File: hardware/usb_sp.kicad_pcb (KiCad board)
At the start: 4 copper layers, 38.1 x 59.7 mm, 48 parts, among them U1 CH32V203C8U6, U10 SN74LVC1G32DBVR, U2 ZD24C02B-MAGMT, U3 32.768kHz, U4 KH-TYPE-C-16P, U5 SD101CWS, U6 CH572D, U7 HX_JN1_27-2X5P_ZZ_H4_9, U8 HX_JN1_27-2X5P_ZZ_H4_9, U9 SN74LVC1G32DBVR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

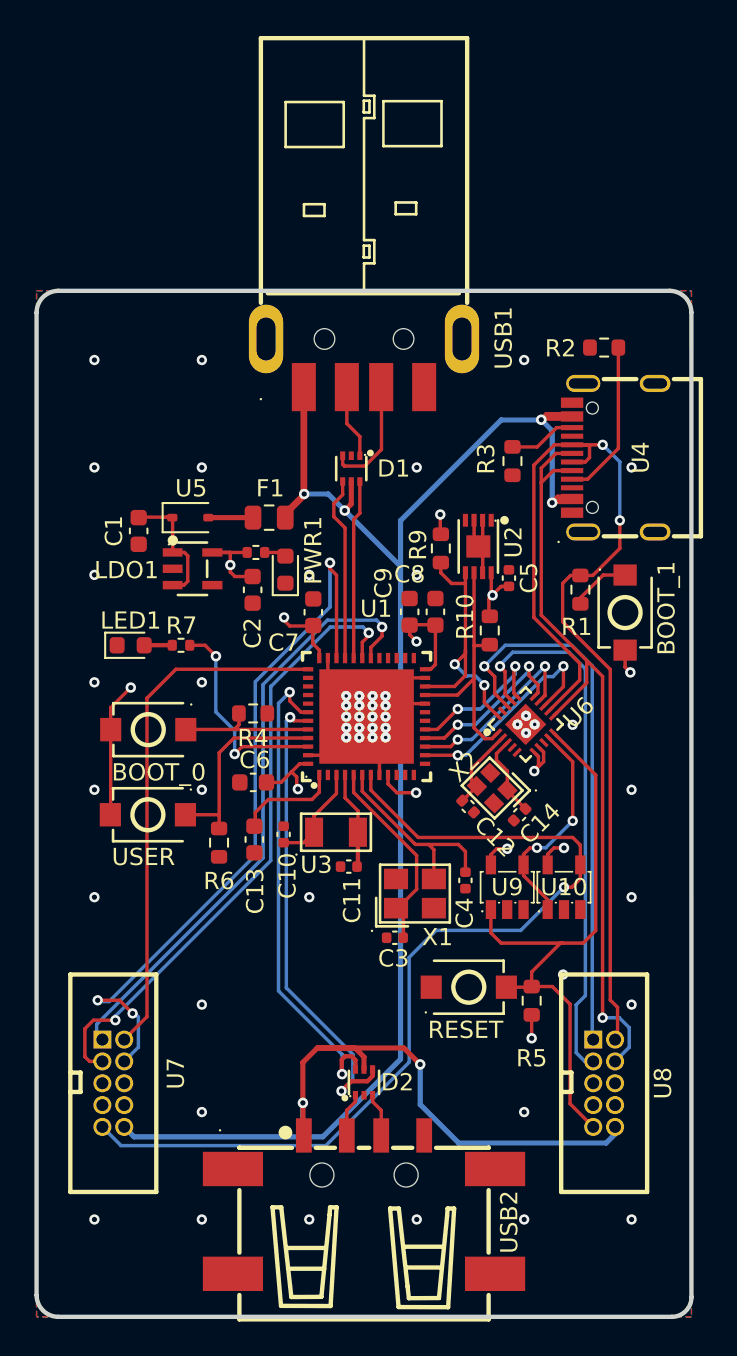
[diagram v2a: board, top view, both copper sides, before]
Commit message: style: improve trace paths
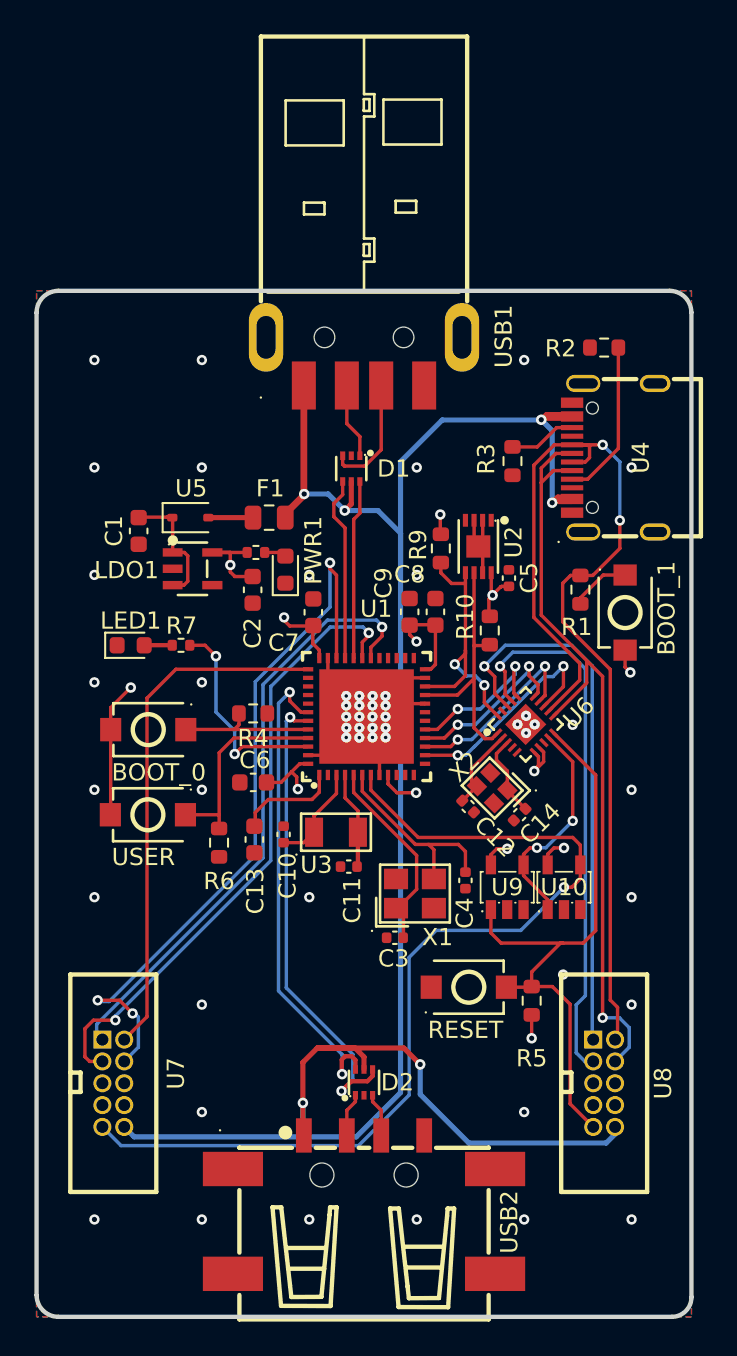
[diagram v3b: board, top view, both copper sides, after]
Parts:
- moved USB1 0.09 mm to (145.9, 70.9)
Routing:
- net VBUS: track 121.1 -> 125.6 mm
- net /CH32V203/RST_CH32: track 54.6 -> 55.7 mm
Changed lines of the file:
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@@
 	(footprint "usb_sp_fp:USB-A-SMD_917-181A102ES60200"
 		(layer "F.Cu")
-		(at 145.879523 70.956735 90)
+		(at 145.879523 70.863526 90)
 		(descr "USB-A-SMD_917-181A102ES60200 footprint")
 		(tags "USB-A-SMD_917-181A102ES60200 footprint C46394")
@@
 	)
 	(segment
-		(start 145.929523 76.950809)
-		(end 144.738727 76.950809)
-		(width 0.2)
-		(layer "F.Cu")
-		(net 40)
-	)
-	(segment
-		(start 146.895523 72.372735)
-		(end 146.895523 75.984809)
+		(start 146.879523 72.356735)
+		(end 146.879523 76.000809)
 		(width 0.2)
 		(layer "F.Cu")
@@
 	)
 	(segment
-		(start 146.900523 72.860335)
-		(end 146.879523 72.839335)
+		(start 144.638523 76.850605)
+		(end 144.638523 76.348745)
 		(width 0.2)
 		(layer "F.Cu")
@@
 	)
 	(segment
-		(start 146.879523 72.356735)
-		(end 146.895523 72.372735)
+		(start 146.879523 72.839335)
+		(end 146.879523 72.356735)
 		(width 0.2)
 		(layer "F.Cu")
@@
 	)
 	(segment
-		(start 146.879523 72.839335)
-		(end 146.879523 72.356735)
+		(start 144.738727 76.950809)
+		(end 144.638523 76.850605)
 		(width 0.2)
 		(layer "F.Cu")
@@
 	)
 	(segment
-		(start 144.638523 76.850605)
-		(end 144.638523 76.348745)
+		(start 146.900523 72.860335)
+		(end 146.879523 72.839335)
 		(width 0.2)
 		(layer "F.Cu")
@@
 	)
 	(segment
-		(start 144.738727 76.950809)
-		(end 144.638523 76.850605)
+		(start 146.879523 76.000809)
+		(end 145.929523 76.950809)
 		(width 0.2)
 		(layer "F.Cu")
@@
 	)
 	(segment
-		(start 146.895523 75.984809)
-		(end 145.929523 76.950809)
+		(start 145.929523 76.950809)
+		(end 144.738727 76.950809)
 		(width 0.2)
 		(layer "F.Cu")
@@
 	)
 	(segment
-		(start 144.879523 74.475809)
-		(end 144.879523 72.356735)
+		(start 145.638523 75.234809)
+		(end 144.879523 74.475809)
 		(width 0.2)
 		(layer "F.Cu")
@@
 	)
 	(segment
-		(start 145.638523 75.234809)
-		(end 144.879523 74.475809)
+		(start 144.879523 74.475809)
+		(end 144.879523 72.263526)
 		(width 0.2)
 		(layer "F.Cu")
@@
 	)
 	(segment
-		(start 154.998123 103.965809)
-		(end 150.070523 103.965809)
+		(start 148.504523 105.531809)
+		(end 148.504523 113.545477)
 		(width 0.2)
 		(layer "B.Cu")
@@
 	)
 	(segment
-		(start 150.070523 103.965809)
-		(end 148.504523 105.531809)
+		(start 145.5656 116.4844)
+		(end 131.74811 116.4844)
 		(width 0.2)
 		(layer "B.Cu")
@@
 	)
 	(segment
-		(start 148.504523 111.632047)
-		(end 143.65217 116.4844)
+		(start 154.998123 103.965809)
+		(end 150.070523 103.965809)
 		(width 0.2)
 		(layer "B.Cu")
@@
 	)
 	(segment
-		(start 148.504523 105.531809)
-		(end 148.504523 111.632047)
+		(start 131.74811 116.4844)
+		(end 130.659521 115.395811)
 		(width 0.2)
 		(layer "B.Cu")
@@
 	)
 	(segment
-		(start 131.74811 116.4844)
-		(end 130.659521 115.395811)
+		(start 148.504523 113.545477)
+		(end 145.5656 116.4844)
 		(width 0.2)
 		(layer "B.Cu")
@@
 	)
 	(segment
-		(start 143.65217 116.4844)
-		(end 131.74811 116.4844)
+		(start 150.070523 103.965809)
+		(end 148.504523 105.531809)
 		(width 0.2)
 		(layer "B.Cu")
@@
 	)
 	(segment
-		(start 142.37965 78.650682)
-		(end 141.259523 79.770809)
-		(width 0.4)
-		(layer "F.Cu")
-		(net 69)
-	)
-	(segment
-		(start 141.259523 79.770809)
-		(end 141.259523 79.950809)
-		(width 0.4)
-		(layer "F.Cu")
-		(net 69)
-	)
-	(segment
 		(start 157.153388 78.755409)
 		(end 157.943313 78.755409)
@@
 	)
 	(segment
-		(start 142.37965 72.839335)
-		(end 142.37965 78.650682)
-		(width 0.4)
-		(layer "F.Cu")
-		(net 69)
-	)
-	(segment
 		(start 142.323523 111.641009)
 		(end 142.323523 116.081009)
@@
 	)
 	(segment
+		(start 142.37965 78.650682)
+		(end 141.259523 79.770809)
+		(width 0.4)
+		(layer "F.Cu")
+		(net 69)
+	)
+	(segment
 		(start 156.190952 74.256845)
 		(end 156.275516 74.172281)
@@
 	)
 	(segment
+		(start 141.259523 79.770809)
+		(end 141.259523 79.950809)
+		(width 0.4)
+		(layer "F.Cu")
+		(net 69)
+	)
+	(segment
 		(start 145.879523 111.327009)
 		(end 145.358523 110.806009)
@@
 	)
 	(segment
+		(start 142.37965 72.263526)
+		(end 142.37965 78.650682)
+		(width 0.4)
+		(layer "F.Cu")
+		(net 69)
+	)
+	(segment
 		(start 148.194809 110.806009)
 		(end 143.158523 110.806009)
@@
 	)
 	(segment
-		(start 148.004523 82.785809)
-		(end 144.757523 79.538809)
+		(start 149.1488 111.76)
+		(end 149.1488 113.4988)
 		(width 0.3)
 		(layer "B.Cu")
@@
 	)
 	(segment
-		(start 160.484523 115.816677)
-		(end 160.484523 115.395809)
+		(start 148.004523 80.854523)
+		(end 146.688809 79.538809)
 		(width 0.3)
 		(layer "B.Cu")
@@
 	)
 	(segment
-		(start 156.825952 74.891845)
-		(end 156.203707 74.2696)
+		(start 142.354523 115.9764)
+		(end 132.510112 115.9764)
 		(width 0.3)
 		(layer "B.Cu")
@@
 	)
 	(segment
-		(start 142.354523 115.9764)
-		(end 132.510112 115.9764)
+		(start 148.004523 76.695477)
+		(end 148.004523 82.785809)
 		(width 0.3)
 		(layer "B.Cu")
@@
 	)
 	(segment
-		(start 148.004523 111.450809)
-		(end 148.004523 82.785809)
+		(start 156.825952 79.082845)
+		(end 156.825952 74.891845)
 		(width 0.3)
 		(layer "B.Cu")
@@
 	)
 	(segment
-		(start 148.004523 80.123809)
-		(end 148.004523 82.785809)
+		(start 156.203707 74.2696)
+		(end 150.4304 74.2696)
 		(width 0.3)
 		(layer "B.Cu")
@@
 	)
 	(segment
-		(start 142.40065 78.575809)
-		(end 143.794523 78.575809)
+		(start 142.354523 115.9764)
+		(end 145.4236 115.9764)
 		(width 0.3)
 		(layer "B.Cu")
@@
 	)
 	(segment
-		(start 151.384 116.332)
+		(start 145.4236 115.9764)
+		(end 148.004523 113.395477)
+		(width 0.3)
+		(layer "B.Cu")
+		(net 69)
+	)
+	(segment
+		(start 151.982 116.332)
 		(end 159.9692 116.332)
 		(width 0.3)
@@
 	)
 	(segment
-		(start 142.354523 115.9764)
-		(end 143.478932 115.9764)
+		(start 146.688809 79.538809)
+		(end 144.757523 79.538809)
 		(width 0.3)
 		(layer "B.Cu")
@@
 	)
 	(segment
-		(start 143.478932 115.9764)
-		(end 148.004523 111.450809)
+		(start 142.40065 78.575809)
+		(end 143.794523 78.575809)
 		(width 0.3)
 		(layer "B.Cu")
@@
 	)
 	(segment
-		(start 153.858732 74.2696)
-		(end 148.004523 80.123809)
+		(start 160.484523 115.816677)
+		(end 160.484523 115.395809)
 		(width 0.3)
 		(layer "B.Cu")
@@
 	)
 	(segment
-		(start 156.825952 79.082845)
-		(end 156.825952 74.891845)
+		(start 159.9692 116.332)
+		(end 160.484523 115.816677)
 		(width 0.3)
 		(layer "B.Cu")
@@
 	)
 	(segment
-		(start 149.1488 114.0968)
-		(end 151.384 116.332)
+		(start 148.004523 82.785809)
+		(end 148.004523 80.854523)
 		(width 0.3)
 		(layer "B.Cu")
@@
 	)
 	(segment
-		(start 149.1488 111.76)
-		(end 149.1488 114.0968)
+		(start 148.004523 113.395477)
+		(end 148.004523 82.785809)
 		(width 0.3)
 		(layer "B.Cu")
@@
 	)
 	(segment
-		(start 156.203707 74.2696)
-		(end 153.858732 74.2696)
+		(start 150.4304 74.2696)
+		(end 148.004523 76.695477)
+		(width 0.3)
+		(layer "B.Cu")
+		(net 69)
+	)
+	(segment
+		(start 149.1488 113.4988)
+		(end 151.982 116.332)
 		(width 0.3)
 		(layer "B.Cu")
@@
 	)
 	(segment
-		(start 159.9692 116.332)
-		(end 160.484523 115.816677)
+		(start 156.825952 74.891845)
+		(end 156.203707 74.2696)
 		(width 0.3)
 		(layer "B.Cu")
